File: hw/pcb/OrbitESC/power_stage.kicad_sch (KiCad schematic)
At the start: 41 parts, among them U5 DRV8300DRGER

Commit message: Sync PCB updates
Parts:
- added C44: 1uF, Capacitor_SMD:C_0402_1005Metric, symbol Device:C
- added R11: 33, Resistor_SMD:R_0402_1005Metric, symbol Device:R_US
- added R5: 2.0k, Resistor_SMD:R_0402_1005Metric, symbol Device:R_US
- C14: value 2.2uF -> 33nF; footprint Capacitor_SMD:C_0805_2012Metric -> Capacitor_SMD:C_0402_1005Metric; JLCPCB C49217 -> C1585
- C30: value 100nF -> 1uF; JLCPCB C307331 -> C52923
- R21, R22: value 10k -> 100k; JLCPCB C25744 -> C25741
- gave numbers to parts that had none: 8
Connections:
- net GND: now also C44.2; no longer C14.2
- net ISenseVRef: now also R11.1, R5.1; no longer U4.1
- net at R21.1, R22.2, U4.3 (+): now also C44.1
- net at C14.1: now also U4.2 (-), R5.2
- new net: C14.2, R11.2, U4.1
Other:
- moved on the sheet: C12, C13, C16, C17, C18, C19, C20, C21, C31, C42, C43, R21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

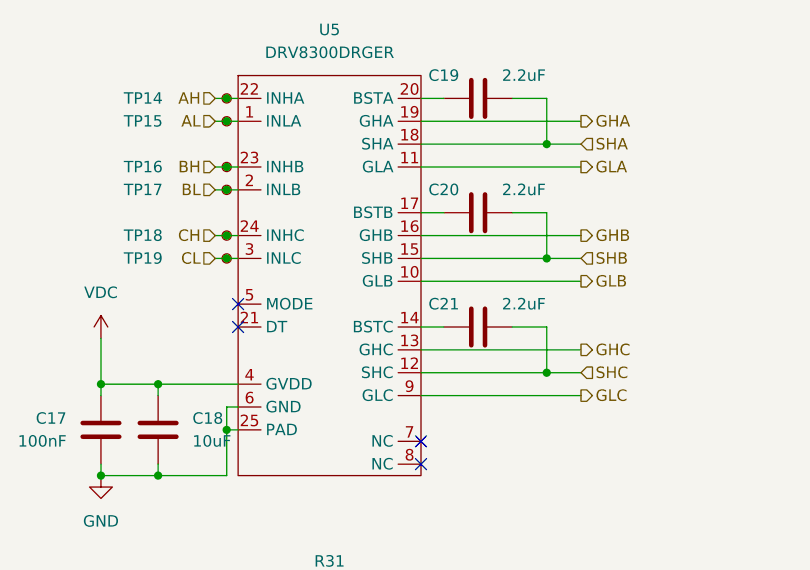
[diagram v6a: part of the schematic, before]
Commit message: Route analogs and starting power stage
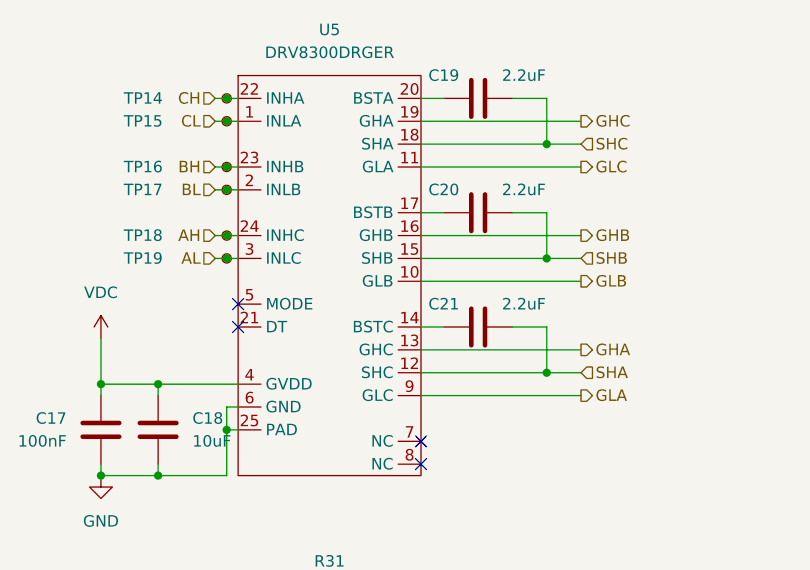
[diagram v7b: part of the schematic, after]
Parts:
- U5: footprint Package_DFN_QFN:VQFN-24-1EP_4x4mm_P0.5mm_EP2.45x2.45mm_ThermalVias -> Package_DFN_QFN:VQFN-24-1EP_4x4mm_P0.5mm_EP2.45x2.45mm
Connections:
- net AH: now also TP18.1, U5.24 (INHC); no longer TP14.1, U5.22 (INHA)
- net AL: now also TP19.1, U5.3 (INLC); no longer TP15.1, U5.1 (INLA)
- net CH: now also TP14.1, U5.22 (INHA); no longer TP18.1, U5.24 (INHC)
- net CL: now also TP15.1, U5.1 (INLA); no longer TP19.1, U5.3 (INLC)
- net GHA: now also U5.13 (GHC); no longer U5.19 (GHA)
- net GHC: now also U5.19 (GHA); no longer U5.13 (GHC)
- net GLA: now also U5.9 (GLC); no longer U5.11 (GLA)
- net GLC: now also U5.11 (GLA); no longer U5.9 (GLC)
- net SHA: now also C21.2, U5.12 (SHC); no longer C19.2, U5.18 (SHA)
- net SHC: now also C19.2, U5.18 (SHA); no longer C21.2, U5.12 (SHC)
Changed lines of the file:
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@@
     (effects (font (size 1.27 1.27)) (justify left))
   )
-  (hierarchical_label "CH" (shape input) (at 135.255 38.735 180)
+  (hierarchical_label "CH" (shape input) (at 135.255 23.495 180)
     (effects (font (size 1.27 1.27)) (justify right))
   )
@@
     (effects (font (size 1.27 1.27)) (justify left))
   )
-  (hierarchical_label "GLA" (shape output) (at 175.895 31.115 0)
-    (effects (font (size 1.27 1.27)) (justify left))
-  )
-  (hierarchical_label "SHC" (shape input) (at 175.895 53.975 0)
+  (hierarchical_label "GLA" (shape output) (at 175.895 56.515 0)
+    (effects (font (size 1.27 1.27)) (justify left))
+  )
+  (hierarchical_label "SHC" (shape input) (at 175.895 28.575 0)
     (effects (font (size 1.27 1.27)) (justify left))
   )
@@
     (effects (font (size 1.27 1.27)) (justify right))
   )
-  (hierarchical_label "GHC" (shape output) (at 175.895 51.435 0)
-    (effects (font (size 1.27 1.27)) (justify left))
-  )
-  (hierarchical_label "GHA" (shape output) (at 175.895 26.035 0)
+  (hierarchical_label "GHC" (shape output) (at 175.895 26.035 0)
+    (effects (font (size 1.27 1.27)) (justify left))
+  )
+  (hierarchical_label "GHA" (shape output) (at 175.895 51.435 0)
     (effects (font (size 1.27 1.27)) (justify left))
   )
@@
     (effects (font (size 1.27 1.27)) (justify left))
   )
-  (hierarchical_label "SHA" (shape input) (at 175.895 28.575 0)
+  (hierarchical_label "SHA" (shape input) (at 175.895 53.975 0)
     (effects (font (size 1.27 1.27)) (justify left))
   )
@@
     (effects (font (size 1.27 1.27)) (justify left))
   )
-  (hierarchical_label "AH" (shape input) (at 135.255 23.495 180)
+  (hierarchical_label "AH" (shape input) (at 135.255 38.735 180)
     (effects (font (size 1.27 1.27)) (justify right))
   )
@@
     (effects (font (size 1.27 1.27)) (justify left))
   )
-  (hierarchical_label "CL" (shape input) (at 135.255 41.275 180)
+  (hierarchical_label "CL" (shape input) (at 135.255 26.035 180)
     (effects (font (size 1.27 1.27)) (justify right))
   )
@@
     (effects (font (size 1.27 1.27)) (justify left))
   )
-  (hierarchical_label "AL" (shape input) (at 135.255 26.035 180)
-    (effects (font (size 1.27 1.27)) (justify right))
-  )
-  (hierarchical_label "GLC" (shape output) (at 175.895 56.515 0)
+  (hierarchical_label "AL" (shape input) (at 135.255 41.275 180)
+    (effects (font (size 1.27 1.27)) (justify right))
+  )
+  (hierarchical_label "GLC" (shape output) (at 175.895 31.115 0)
     (effects (font (size 1.27 1.27)) (justify left))
   )
@@
     (property "Reference" "U5" (id 0) (at 147.955 15.875 0))
     (property "Value" "DRV8300DRGER" (id 1) (at 147.955 18.415 0))
-    (property "Footprint" "Package_DFN_QFN:VQFN-24-1EP_4x4mm_P0.5mm_EP2.45x2.45mm_ThermalVias" (id 2) (at 145.415 33.655 0)
-      (effects (font (size 1.27 1.27)) hide)
-    )
+    (property "Footprint" "Package_DFN_QFN:VQFN-24-1EP_4x4mm_P0.5mm_EP2.45x2.45mm" (id 2) (at 145.415 33.655 0)
+      (effects (font (size 1.27 1.27)) hide)
+    )

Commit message: Finalize V2 PCB
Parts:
- added TP3: BL, TestPoint:TestPoint_Pad_D1.0mm, symbol Connector:TestPoint_Small
- added TP4, TP6, TP7, TP8: AH, TestPoint:TestPoint_Pad_D1.0mm, symbol Connector:TestPoint_Small
- C12, C13, C16, C17, C31, C42, C43: JLCPCB C307331 -> (none); LCSC (none) -> C307331
- C14: JLCPCB C1585 -> (none); LCSC (none) -> C1585
- C18: JLCPCB C440198 -> (none); LCSC (none) -> C440198
- C19, C20, C21: JLCPCB C49217 -> (none); LCSC (none) -> C49217
- C30, C44: JLCPCB C52923 -> (none); LCSC (none) -> C52923
- R11: JLCPCB C25105 -> (none); LCSC (none) -> C25105
- R21, R22: JLCPCB C25741 -> (none); LCSC (none) -> C25741
- R23, R25, R28, R30, R31, R34, R47: JLCPCB C25744 -> (none); LCSC (none) -> C25744
- R24: JLCPCB C25867 -> (none); LCSC (none) -> C25867
- R26, R27, R32, R33, R35, R36: JLCPCB C11702 -> (none); LCSC (none) -> C11702
- R5: JLCPCB C4109 -> (none); LCSC (none) -> C4109
- U13, U14, U4, U6: JLCPCB C1849429 -> (none); LCSC (none) -> C1849429
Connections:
- net +3.3VADC: now also TP6.1
- net GND: now also TP3.1
- net IA: now also TP8.1
- net IB: now also TP7.1
- net IC: now also TP4.1
